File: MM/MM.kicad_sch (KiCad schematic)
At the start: 20 parts, among them SW1 C2890358, SW2 C2890358, U1 DRV8833PWPR, U2 DRV8833PWPR, U3 TP5100

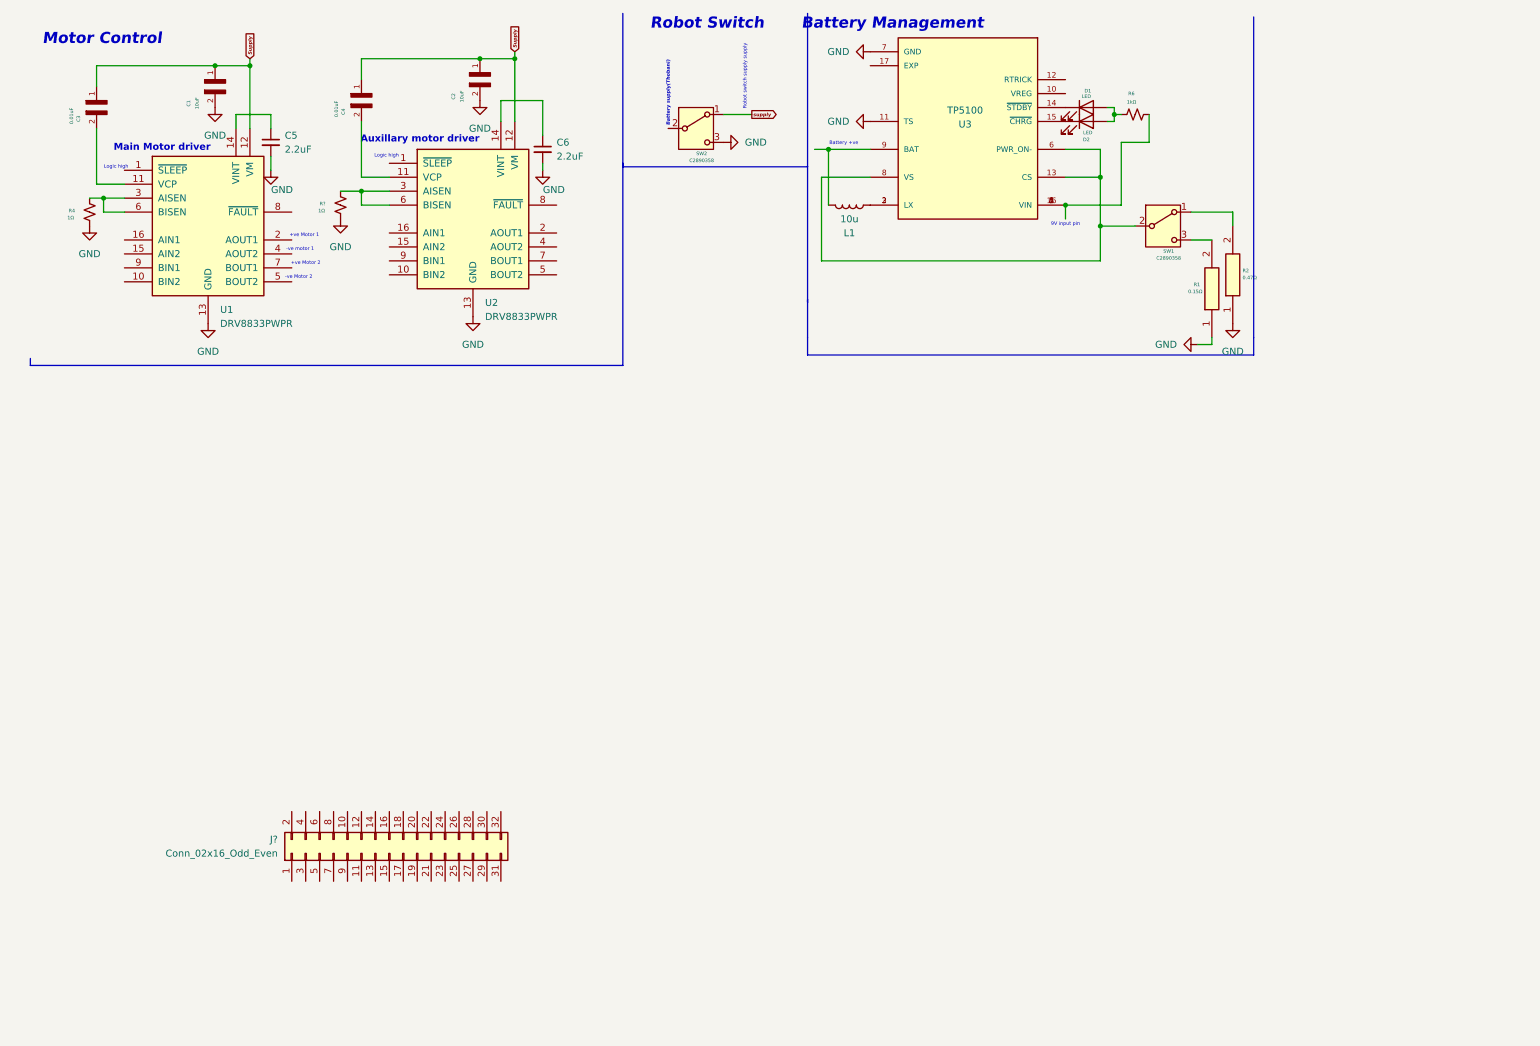
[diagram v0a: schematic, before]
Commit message: Add 3.3V and 5V power regulation using XL1509 regulators
- Implemented XL1509-3.3 and XL1509-5.0 with 9V input from Pin 22 (USB-C)
- 5V output routed to MM Pin 20 and TPS2042D
- 3.3V output used for INA219 and I2C pullups
- Added input/output filtering caps, inductors, and Schottky diodes
- EN pins pulled low via resistors to enable regulators
- FB pins tied to VOUT for fixed-output operation
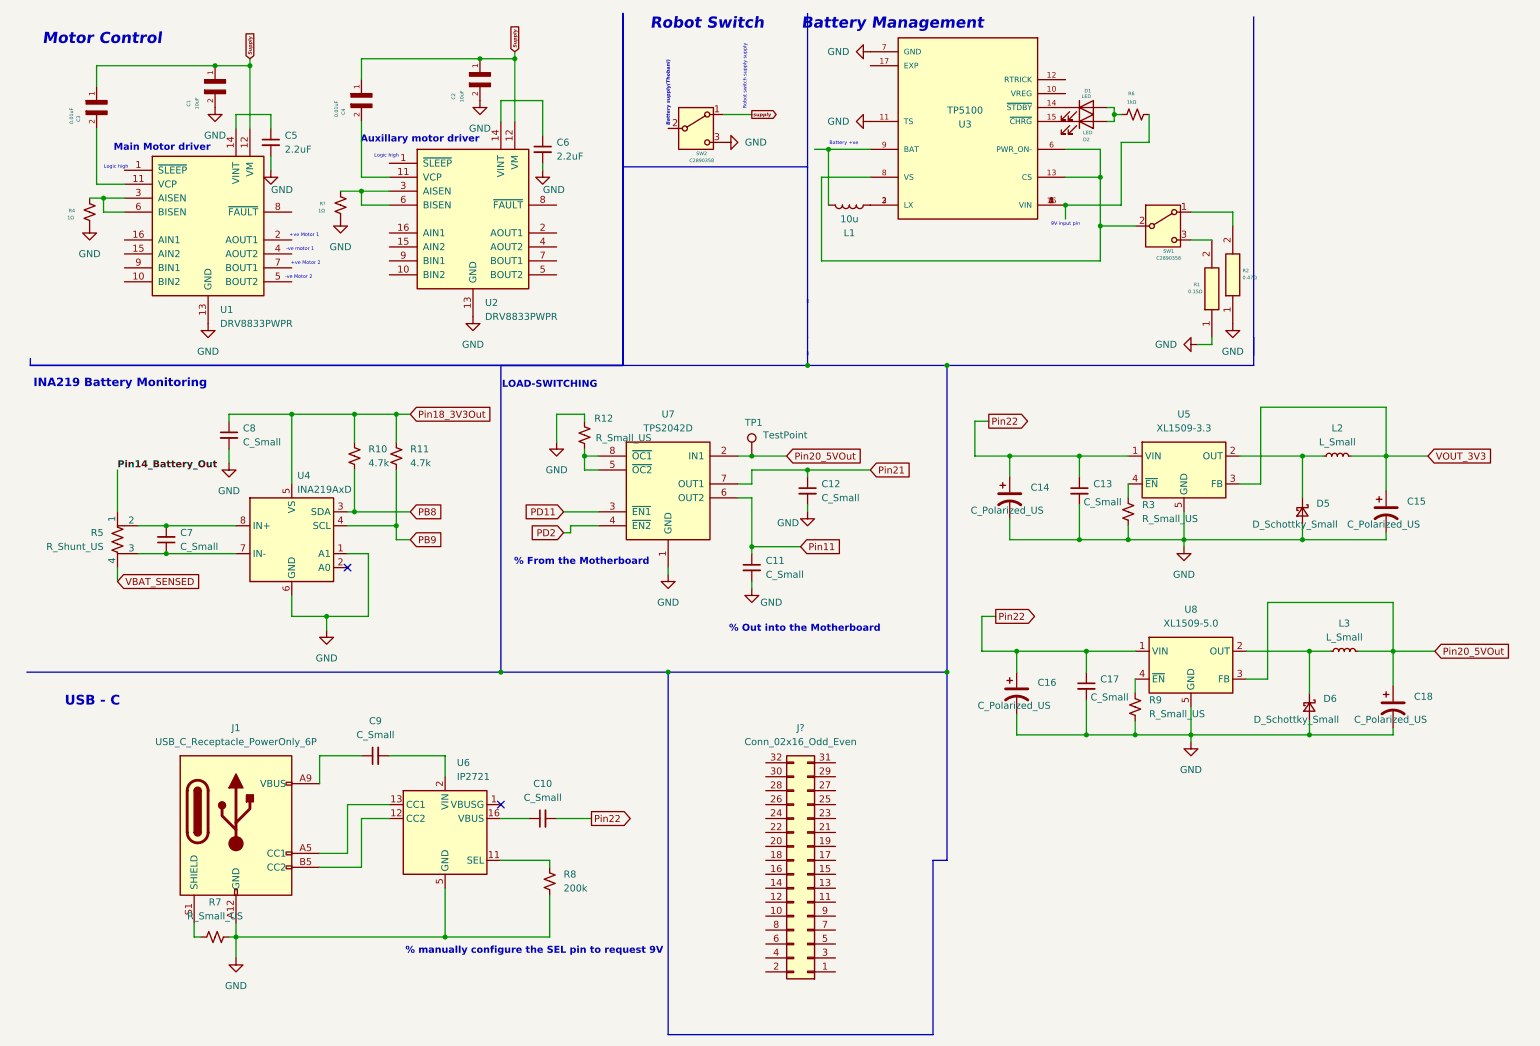
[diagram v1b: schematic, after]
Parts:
- added C10, C11, C12, C13, C17, C7, C8, C9: C_Small, symbol Device:C_Small
- added C14, C15, C16, C18: C_Polarized_US, symbol Device:C_Polarized_US
- added D5, D6: D_Schottky_Small, symbol Device:D_Schottky_Small
- added J1: USB_C_Receptacle_PowerOnly_6P, symbol Connector:USB_C_Receptacle_PowerOnly_6P
- added L2, L3: L_Small, symbol Device:L_Small
- added R10, R11: 4.7k, symbol Device:R_Small_US
- added R12, R3, R7, R9: R_Small_US, symbol Device:R_Small_US
- added R5: R_Shunt_US, symbol Device:R_Shunt_US
- added R8: 200k, symbol Device:R_Small_US
- added TP1: TestPoint, symbol Connector:TestPoint
- added U4: INA219AxD, Package_SO:SOIC-8_3.9x4.9mm_P1.27mm, symbol Sensor_Energy:INA219AxD
- added U5: XL1509-3.3, Package_SO:SOIC-8_3.9x4.9mm_P1.27mm, symbol Regulator_Switching:XL1509-3.3
- added U6: IP2721, Package_SO:TSSOP-16_4.4x5mm_P0.65mm, symbol Interface_USB:IP2721
- added U7: TPS2042D, Package_SO:SOIC-8_3.9x4.9mm_P1.27mm, symbol Power_Management:TPS2042D
- added U8: XL1509-5.0, Package_SO:SOIC-8_3.9x4.9mm_P1.27mm, symbol Regulator_Switching:XL1509-5.0
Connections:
- net GND: now also C11.2, C12.2, C13.2, C14.2, C15.2, C16.2, C17.2, C18.2, C8.2, D5.2 (A), D6.2 (A), J1.A12 (GND), J1.B12 (GND), R12.1, R3.2, R7.2, R8.2, R9.2, U4.1 (A1), U4.6 (GND), U5.5 (GND), U5.6 (GND), U5.7 (GND), U5.8 (GND), U6.5 (GND), U7.1 (GND), U8.5 (GND), U8.6 (GND), U8.7 (GND), U8.8 (GND)
- new net: R9.1, U8.4 (~{EN})
- new net: D5.1 (K), L2.1, U5.2 (OUT)
- new net: C10.1, U6.16 (VBUS)
- new net: C9.1, J1.A9 (VBUS), J1.B9 (VBUS)
- new net: C9.2, U6.2 (VIN)
- new net: D6.1 (K), L3.1, U8.2 (OUT)
- new net: J1.A5 (CC1), U6.13 (CC1)
- new net: J1.B5 (CC2), U6.12 (CC2)
- new net: J1.S1 (SHIELD), R7.1
- new net: R8.1, U6.11 (SEL)
- new net: R12.2, U7.5 (~{OC2}), U7.8 (~{OC1})
- new net: C7.1, R5.3, U4.7 (IN-)
- new net: C7.2, R5.2, U4.8 (IN+)
- new net: R3.1, U5.4 (~{EN})
- new net PB8: R10.2, U4.3 (SDA)
- new net PB9: R11.2, U4.4 (SCL)
- new net PD11: U7.3 (~{EN1})
- new net PD2 : U7.4 (~{EN2})
- new net Pin11: C11.1, U7.6 (OUT2)
- new net Pin14_Battery_Out: R5.1
- new net Pin18_3V3Out: C8.1, R10.1, R11.1, U4.5 (VS)
- new net Pin20_5VOut: C18.1, L3.2, TP1.1, U7.2 (IN1), U8.3 (FB)
- new net Pin21: C12.1, U7.7 (OUT1)
- new net Pin22: C10.2, C13.1, C14.1, C16.1, C17.1, U5.1 (VIN), U8.1 (VIN)
- new net VBAT_SENSED: R5.4
- new net VOUT_3V3: C15.1, L2.2, U5.3 (FB)
- no-connect marks 0 -> 2
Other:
- note added: "% From the Motherboard"
- note added: "% Out into the Motherboard"
- note added: "% manually configure the SEL pin to request 9V"
- note added: "INA219 Battery Monitoring"
- note added: "LOAD-SWITCHING"
- note added: "USB - C"
- moved on the sheet: J?

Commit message: Update supporting components for all ICs to JLCPCB-compatible parts (caps, resistors, inductors, diodes)
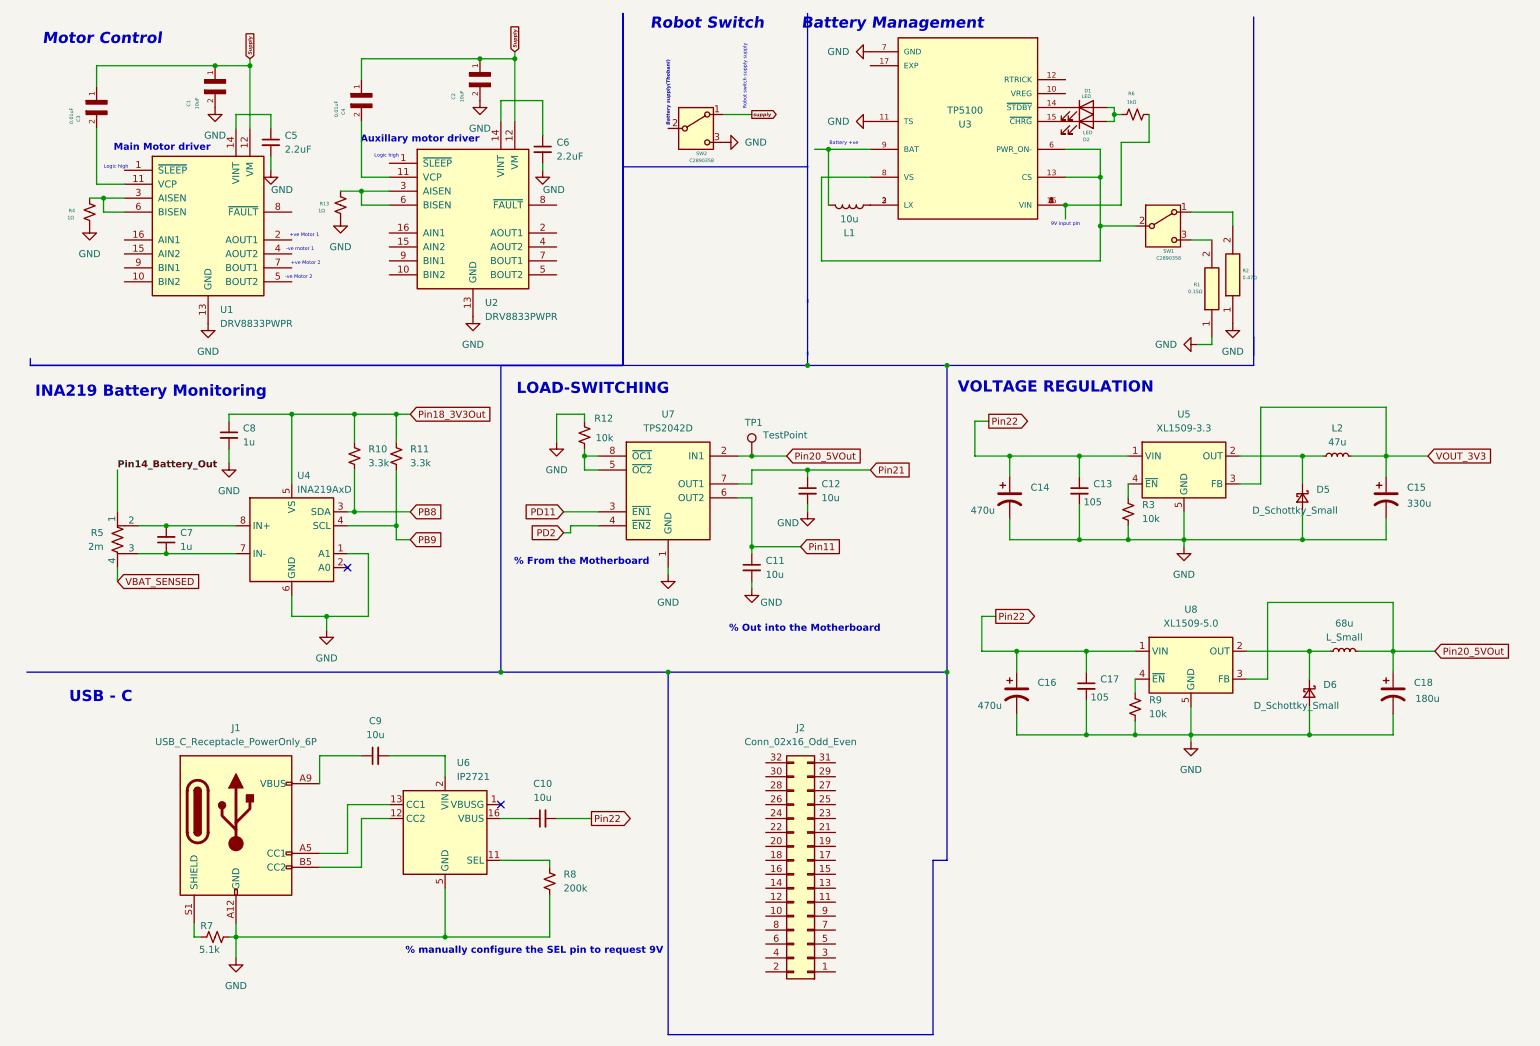
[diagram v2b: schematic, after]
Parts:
- C10, C11, C12, C9: value C_Small -> 10u
- C13, C17: value C_Small -> 105
- C14, C16: value C_Polarized_US -> 470u
- C15: value C_Polarized_US -> 330u
- C18: value C_Polarized_US -> 180u
- C7, C8: value C_Small -> 1u
- L2: value L_Small -> 47u
- R10, R11: value 4.7k -> 3.3k
- R12, R3, R9: value R_Small_US -> 10k
- R5: value R_Shunt_US -> 2m
- R7: value R_Small_US -> 5.1k
- gave numbers to parts that had none: 2
- renumbered L3 to 68u
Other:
- note added: "VOLTAGE REGULATION"
- moved on the sheet: C15, C18, D5, D6
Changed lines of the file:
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@@
 	(text "LOAD-SWITCHING"
 		(exclude_from_sim no)
-		(at 106.68 79.756 0)
+		(at 114.554 80.518 0)
 		(effects
 			(font
-				(size 1.27 1.27)
+				(size 2.032 2.032)
 				(thickness 0.254)
 				(bold yes)
@@
 		)
 	)
+	(text "VOLTAGE REGULATION"
+		(exclude_from_sim no)
+		(at 198.882 80.264 0)
+		(effects
+			(font
+				(size 2.032 2.032)
+				(thickness 0.254)
+				(bold yes)
+			)
+		)
+	)
 	(text "Battery Management\n"
 		(exclude_from_sim no)
@@
 	(text "USB - C"
 		(exclude_from_sim no)
-		(at 23.368 137.414 0)
+		(at 24.892 136.652 0)
 		(effects
 			(font
-				(size 1.778 1.778)
+				(size 2.032 2.032)
 				(thickness 0.2794)
 				(bold yes)
@@
 	(text "INA219 Battery Monitoring"
 		(exclude_from_sim no)
-		(at 28.448 79.502 0)
+		(at 34.036 81.026 0)
 		(effects
 			(font
-				(size 1.524 1.524)
+				(size 2.032 2.032)
 				(thickness 0.254)
 				(bold yes)
@@
 	(wire
 		(pts
-			(xy 260.35 128.27) (xy 260.35 134.62)
+			(xy 260.35 128.27) (xy 260.35 132.08)
 		)
 		(stroke
@@
 	(wire
 		(pts
-			(xy 260.35 142.24) (xy 260.35 143.51)
+			(xy 260.35 139.7) (xy 260.35 143.51)
 		)
 		(stroke
@@
 	(wire
 		(pts
-			(xy 245.11 140.97) (xy 245.11 143.51)
+			(xy 245.11 138.43) (xy 245.11 143.51)
 		)
 		(stroke
@@
 	(wire
 		(pts
-			(xy 259.08 92.71) (xy 259.08 99.06)
+			(xy 259.08 92.71) (xy 259.08 96.52)
 		)
 		(stroke
@@
 	(wire
 		(pts
-			(xy 243.84 105.41) (xy 243.84 107.95)
+			(xy 243.84 102.87) (xy 243.84 107.95)
 		)
 		(stroke
@@
 	(wire
 		(pts
-			(xy 245.11 128.27) (xy 245.11 135.89)
+			(xy 245.11 128.27) (xy 245.11 133.35)
 		)
 		(stroke
@@
 	(wire
 		(pts
-			(xy 243.84 92.71) (xy 243.84 100.33)
+			(xy 243.84 92.71) (xy 243.84 97.79)
 		)
 		(stroke
@@
 	(wire
 		(pts
-			(xy 259.08 106.68) (xy 259.08 107.95)
+			(xy 259.08 104.14) (xy 259.08 107.95)
 		)
 		(stroke
@@
 			)
 		)
-		(property "Value" "R_Small_US"
+		(property "Value" "10k"
 			(at 215.9 139.6999 0)
 			(effects
@@
 			)
 		)
-		(property "Value" "L_Small"
+		(property "Value" "47u"
 			(at 250.19 90.17 90)
 			(effects
@@
 			)
 		)
-		(property "Value" "C_Small"
+		(property "Value" "1u"
 			(at 50.8 90.1762 0)
 			(effects
@@
 			)
 		)
-		(property "Value" "C_Small"
+		(property "Value" "105"
 			(at 203.962 101.092 0)
 			(effects
@@
 			)
 		)
-		(property "Value" "C_Small"
+		(property "Value" "10u"
 			(at 105.4163 154.94 90)
 			(effects
@@
 			)
 		)
-		(property "Value" "C_Small"
+		(property "Value" "10u"
 			(at 74.9363 143.51 90)
 			(effects
@@
 		(dnp no)
 		(fields_autoplaced yes)
-		(property "Reference" "L3"
+		(property "Reference" "68u"
 			(at 251.46 123.19 90)
 			(effects
@@
 			(project "MM"
 				(path "/c08f2f70-f64e-46c6-9738-1b2adc0f0e4b"
-					(reference "L3")
+					(reference "68u")
 					(unit 1)
 				)
@@
 			)
 		)
-		(property "Value" "R_Small_US"
+		(property "Value" "10k"
 			(at 115.062 89.408 0)
 			(effects
@@
 			)
 		)
-		(property "Value" "C_Polarized_US"
+		(property "Value" "470u"
 			(at 184.658 138.176 0)
 			(effects
@@
 			)
 		)
-		(property "Value" "R_Shunt_US"
+		(property "Value" "2m"
 			(at 25.4 109.2199 0)
 			(effects
@@
 			)
 		)
-		(property "Value" "4.7k"
+		(property "Value" "3.3k"
 			(at 73.66 93.9799 0)
 			(effects
@@
 		(on_board yes)
 		(dnp no)
-		(property "Reference" "R?"
+		(property "Reference" "R13"
 			(at 64.77 46.736 0)
 			(effects
@@
 			(project "MM"
 				(path "/c08f2f70-f64e-46c6-9738-1b2adc0f0e4b"
-					(reference "R?")
+					(reference "R13")
 					(unit 1)
 				)
@@
 		(on_board yes)
 		(dnp no)
-		(fields_autoplaced yes)
 		(property "Reference" "R7"
-			(at 45.72 173.99 90)
+			(at 44.196 178.308 90)
 			(effects
 				(font
@@
 			)
 		)
-		(property "Value" "R_Small_US"
-			(at 45.72 176.53 90)
+		(property "Value" "5.1k"
+			(at 44.704 182.626 90)
 			(effects
 				(font
@@
 		(dnp no)
 		(fields_autoplaced yes)
-		(property "Reference" "J?"
+		(property "Reference" "J2"
 			(at 152.4 142.24 0)
 			(effects
@@
 			(project "MM"
 				(path "/c08f2f70-f64e-46c6-9738-1b2adc0f0e4b"
-					(reference "J?")
+					(reference "J2")
 					(unit 1)
 				)
@@
 			)
 		)
-		(property "Value" "C_Small"
+		(property "Value" "10u"
 			(at 156.21 100.3362 0)
 			(effects
@@
 	(symbol
 		(lib_id "Device:C_Polarized_US")
-		(at 260.35 138.43 0)
+		(at 260.35 135.89 0)
 		(unit 1)
 		(exclude_from_sim no)
@@
 		(dnp no)
 		(property "Reference" "C18"
-			(at 264.16 136.5249 0)
+			(at 264.16 133.9849 0)
 			(effects
 				(font
@@
 			)
 		)
-		(property "Value" "C_Polarized_US"
-			(at 253.238 140.716 0)
+		(property "Value" "180u"
+			(at 264.414 136.906 0)
 			(effects
 				(font
@@
 		)
 		(property "Footprint" ""
-			(at 260.35 138.43 0)
+			(at 260.35 135.89 0)
 			(effects
 				(font
@@
 		)
 		(property "Datasheet" "~"
-			(at 260.35 138.43 0)
+			(at 260.35 135.89 0)
 			(effects
 				(font
@@
 		)
 		(property "Description" "Polarized capacitor, US symbol"
-			(at 260.35 138.43 0)
+			(at 260.35 135.89 0)
 			(effects
 				(font
@@
 			)
 		)
-		(property "Value" "R_Small_US"
+		(property "Value" "10k"
 			(at 214.63 104.1399 0)
 			(effects
@@
 	(symbol
 		(lib_id "Device:C_Polarized_US")
-		(at 259.08 102.87 0)
+		(at 259.08 100.33 0)
 		(unit 1)
 		(exclude_from_sim no)
@@
 		(dnp no)
 		(property "Reference" "C15"
-			(at 262.89 100.9649 0)
+			(at 262.89 98.4249 0)
 			(effects
 				(font
@@
 			)
 		)
-		(property "Value" "C_Polarized_US"
-			(at 251.968 105.156 0)
+		(property "Value" "330u"
+			(at 262.89 101.346 0)
 			(effects
 				(font
@@
 		)
 		(property "Footprint" ""
-			(at 259.08 102.87 0)
+			(at 259.08 100.33 0)
 			(effects
 				(font
@@
 		)
 		(property "Datasheet" "~"
-			(at 259.08 102.87 0)
+			(at 259.08 100.33 0)
 			(effects
 				(font
@@
 		)
 		(property "Description" "Polarized capacitor, US symbol"
-			(at 259.08 102.87 0)
+			(at 259.08 100.33 0)
 			(effects
 				(font
@@
 	(symbol
 		(lib_id "Device:D_Schottky_Small")
-		(at 243.84 102.87 270)
+		(at 243.84 100.33 270)
 		(unit 1)
 		(exclude_from_sim no)
@@
 		(dnp no)
 		(property "Reference" "D5"
-			(at 246.38 101.3459 90)
+			(at 246.38 98.8059 90)
 			(effects
 				(font
@@
 		)
 		(property "Value" "D_Schottky_Small"
-			(at 234.696 105.156 90)
+			(at 234.696 102.616 90)
 			(effects
 				(font
@@
 		)
 		(property "Footprint" ""
-			(at 243.84 102.87 90)
+			(at 243.84 100.33 90)
 			(effects
 				(font
@@
 		)
 		(property "Datasheet" "~"
-			(at 243.84 102.87 90)
+			(at 243.84 100.33 90)
 			(effects
 				(font
@@
 		)
 		(property "Description" "Schottky diode, small symbol"
-			(at 243.84 102.87 0)
+			(at 243.84 100.33 0)
 			(effects
 				(font
@@
 	(symbol
 		(lib_id "Device:D_Schottky_Small")
-		(at 245.11 138.43 270)
+		(at 245.11 135.89 270)
 		(unit 1)
 		(exclude_from_sim no)
@@
 		(dnp no)
 		(property "Reference" "D6"
-			(at 247.65 136.9059 90)
+			(at 247.65 134.3659 90)
 			(effects
 				(font
@@
 		)
 		(property "Value" "D_Schottky_Small"
-			(at 234.95 140.716 90)
+			(at 234.95 138.176 90)
 			(effects
 				(font
@@
 		)
 		(property "Footprint" ""
-			(at 245.11 138.43 90)
+			(at 245.11 135.89 90)
 			(effects
 				(font
@@
 		)
 		(property "Datasheet" "~"
-			(at 245.11 138.43 90)
+			(at 245.11 135.89 90)
 			(effects
 				(font
@@
 		)
 		(property "Description" "Schottky diode, small symbol"
-			(at 245.11 138.43 0)
+			(at 245.11 135.89 0)
 			(effects
 				(font
@@
 			)
 		)
-		(property "Value" "C_Small"
+		(property "Value" "105"
 			(at 205.232 136.652 0)
 			(effects
@@
 			)
 		)
-		(property "Value" "C_Small"
+		(property "Value" "1u"
 			(at 39.37 109.2135 0)
 			(effects
@@
 			)
 		)
-		(property "Value" "C_Small"
+		(property "Value" "10u"
 			(at 146.05 114.3062 0)
 			(effects
@@
 			)
 		)
-		(property "Value" "C_Polarized_US"
+		(property "Value" "470u"
 			(at 183.388 102.616 0)
 			(effects
@@
 			)
 		)
-		(property "Value" "4.7k"
+		(property "Value" "3.3k"
 			(at 81.28 93.9799 0)
 			(effects
